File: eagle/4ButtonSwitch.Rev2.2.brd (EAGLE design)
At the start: 69.8 x 69.8 mm, 46 parts

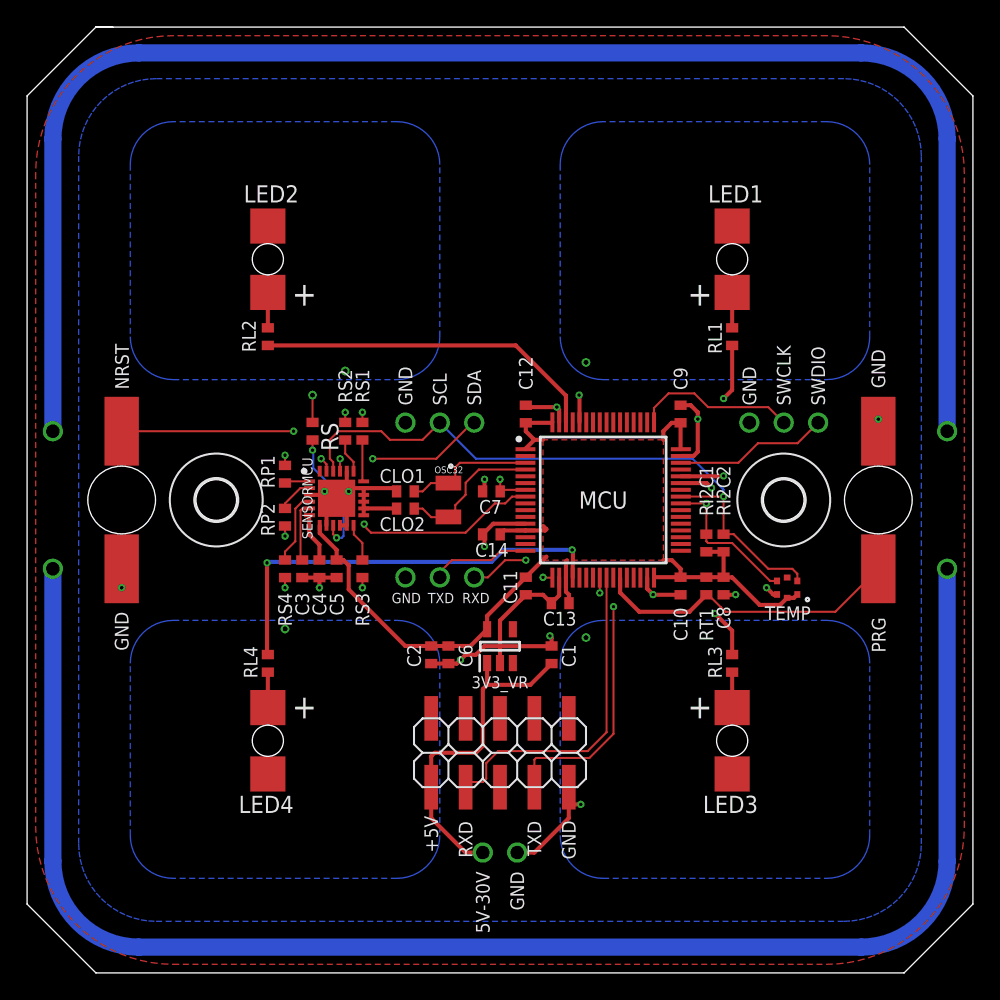
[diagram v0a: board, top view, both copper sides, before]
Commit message: update for cost efficient board manufacturing
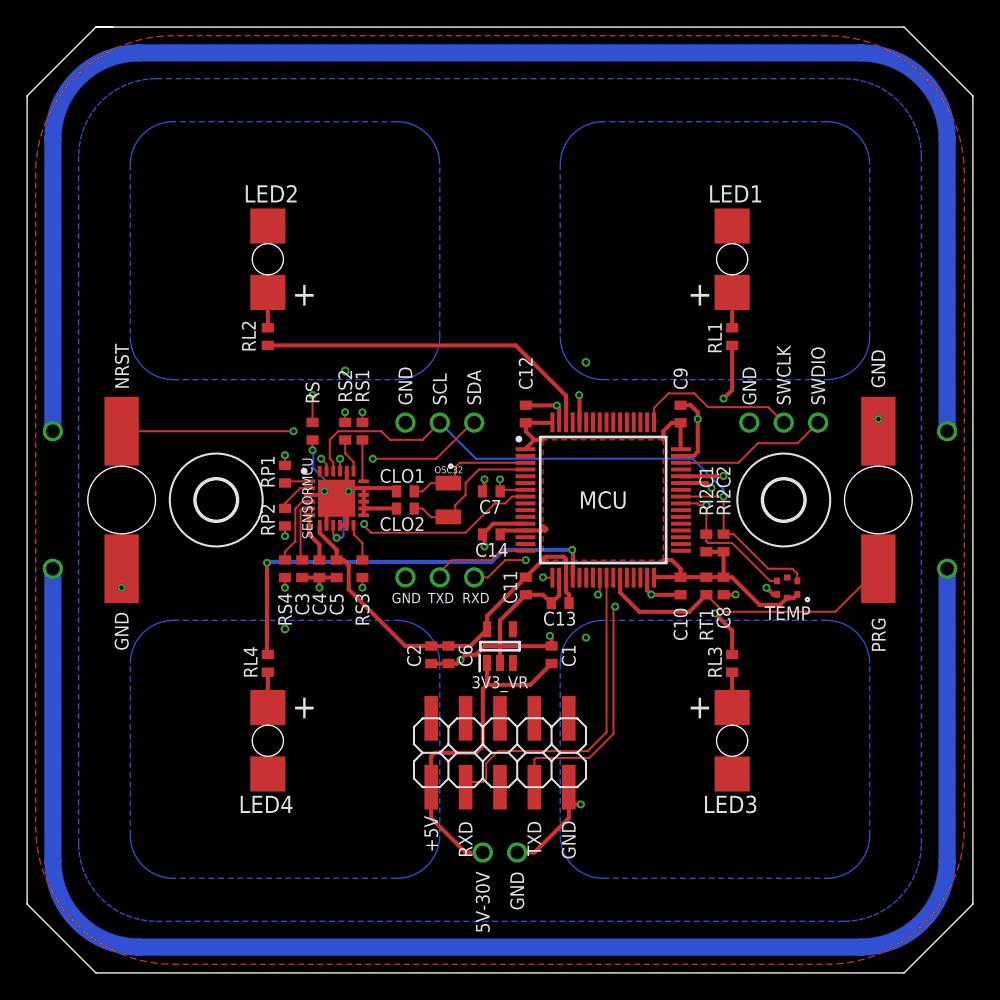
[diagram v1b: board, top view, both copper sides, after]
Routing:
- net GND: track 209.0 -> 207.3 mm
- net +3V3: track 59.1 -> 60.6 mm
- net USART1_TX: track 20.7 -> 21.2 mm
